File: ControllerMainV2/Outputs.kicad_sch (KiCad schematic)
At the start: 25 parts, among them IC20 TMUX6112PWR, IC27 1462039-4, J27 Conn_01x02, Q5 2N7002, T1 Lehle_MZ_P, U12 TL072

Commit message: Added libs
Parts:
- removed J26: (no value), symbol Connector_Generic:Conn_01x02
- removed J27: Conn_01x02, symbol Connector_Generic:Conn_01x02
- added C31: (no value), Capacitor_SMD:C_1206_3216Metric_Pad1.33x1.80mm_HandSolder, symbol Device:C
- added PS1: (no value), symbol SamacSys_Parts:TBA_1-0310
- added Q7: (no value), symbol SamacSys_Parts:EL817S1_A__TU_-F
- added R67: 100k, Resistor_SMD:R_1206_3216Metric_Pad1.30x1.75mm_HandSolder, symbol Device:R
- added R68: (no value), Resistor_SMD:R_1206_3216Metric_Pad1.30x1.75mm_HandSolder, symbol Device:R
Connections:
- net GND: now also PS1.1 (-VIN_(GND)), Q7.3 (E)
- net out2_con: now also Q7.4 (C), R67.2; no longer J_8.4
- net at IC27.3 (COM_1), J_8.1, R21.1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: now also J_8.4, C31.1, PS1.3 (-VOUT)
- net at J_8.5: now also Q7.2 (K)
- new net: C31.2, PS1.4 (+VOUT), R68.1
- new net: Q7.1 (A), R68.2
- new net VDD_3V3: PS1.2 (+VIN_(VCC)), R67.1
- no-connect marks 9 -> 8

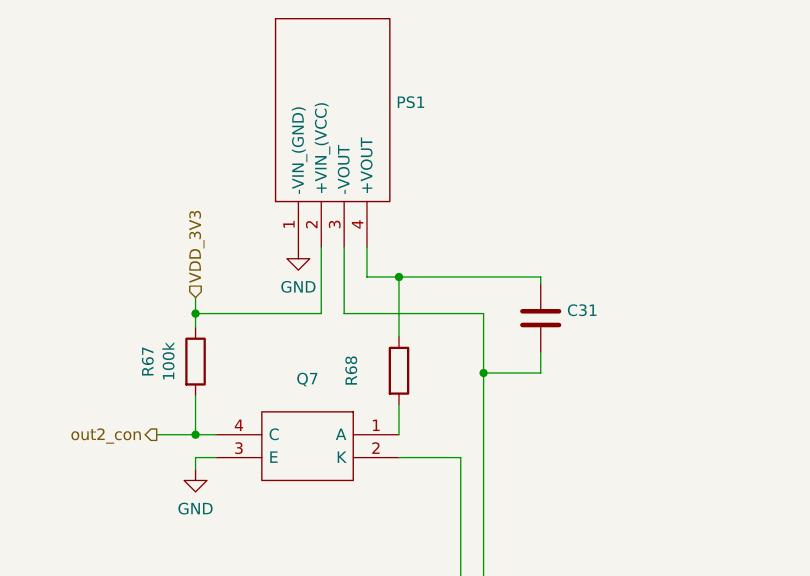
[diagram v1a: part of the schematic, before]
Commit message: Main mostly wired. Push for replacement
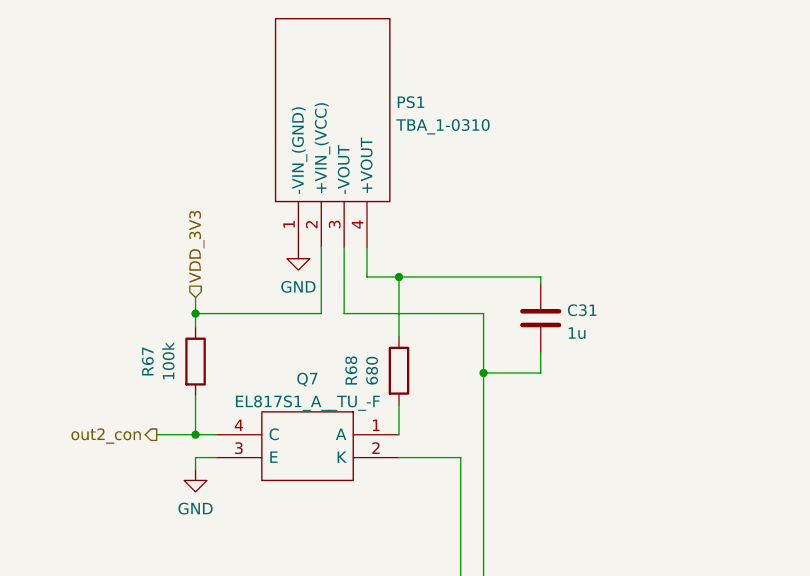
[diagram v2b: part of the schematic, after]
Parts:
- C31: value (none) -> 1u
- PS1: value (none) -> TBA_1-0310; footprint (none) -> SamacSys_Parts:TBA1
- Q7: value (none) -> EL817S1_A__TU_-F; footprint (none) -> SamacSys_Parts:SOP254P1030X390-4N
- R68: value (none) -> 680
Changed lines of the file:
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@@
     (in_bom yes) (on_board yes)
     (property "Reference" "R68" (id 0) (at 240.8682 55.372 90))
-    (property "Value" "" (id 1) (at 243.1796 55.372 90))
+    (property "Value" "680" (id 1) (at 243.1796 55.372 90))
     (property "Footprint" "Resistor_SMD:R_1206_3216Metric_Pad1.30x1.75mm_HandSolder" (id 2) (at 244.348 55.372 90)
       (effects (font (size 1.27 1.27)) hide)
@@
       (effects (font (size 1.27 1.27)) (justify right))
     )
-    (property "Value" "" (id 1) (at 245.8212 28.1182 90)
-      (effects (font (size 1.27 1.27)) (justify right))
-    )
-    (property "Footprint" "" (id 2) (at 232.41 14.986 0)
+    (property "Value" "TBA_1-0310" (id 1) (at 245.8212 28.1182 90)
+      (effects (font (size 1.27 1.27)) (justify right))
+    )
+    (property "Footprint" "SamacSys_Parts:TBA1" (id 2) (at 232.41 14.986 0)
       (effects (font (size 1.27 1.27)) (justify left) hide)
     )
@@
     (in_bom yes) (on_board yes) (fields_autoplaced)
     (property "Reference" "Q7" (id 0) (at 235.966 56.295 0))
-    (property "Value" "" (id 1) (at 235.966 58.8319 0))
-    (property "Footprint" "" (id 2) (at 229.616 59.944 0)
+    (property "Value" "EL817S1_A__TU_-F" (id 1) (at 235.966 58.8319 0))
+    (property "Footprint" "SamacSys_Parts:SOP254P1030X390-4N" (id 2) (at 229.616 59.944 0)
       (effects (font (size 1.27 1.27)) (justify left) hide)
     )
@@
       (effects (font (size 1.27 1.27)) (justify right))
     )
-    (property "Value" "" (id 1) (at 264.795 51.2322 0)
-      (effects (font (size 1.27 1.27)) (justify right))
-    )
+    (property "Value" "1u" (id 1) (at 264.795 51.2322 0)
+      (effects (font (size 1.27 1.27)) (justify right))
+    )

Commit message: Commit for branch change
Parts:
- R67: value 100k -> 10k
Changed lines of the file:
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@@
     (in_bom yes) (on_board yes)
     (property "Reference" "R67" (id 0) (at 218.2622 54.356 90))
-    (property "Value" "100k" (id 1) (at 220.5736 54.356 90))
+    (property "Value" "10k" (id 1) (at 220.5736 54.356 90))
     (property "Footprint" "Resistor_SMD:R_1206_3216Metric_Pad1.30x1.75mm_HandSolder" (id 2) (at 221.742 54.356 90)
       (effects (font (size 1.27 1.27)) hide)

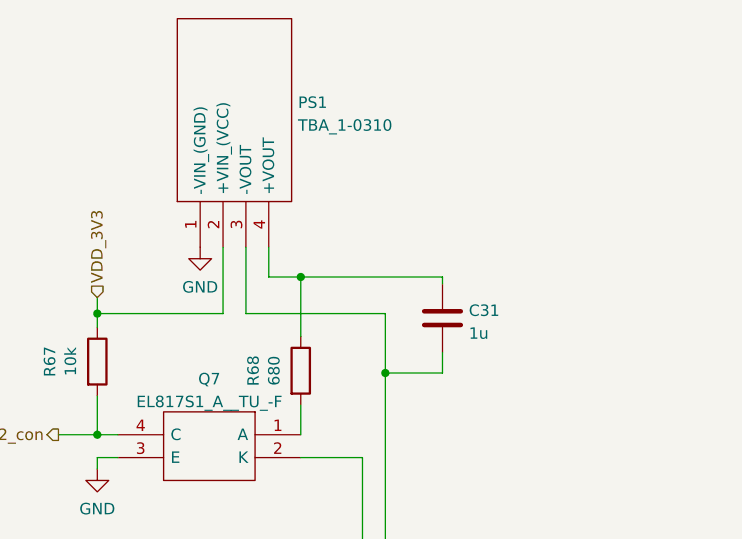
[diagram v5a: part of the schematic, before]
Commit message: Changed main to 8 loop version. Might add buffers later
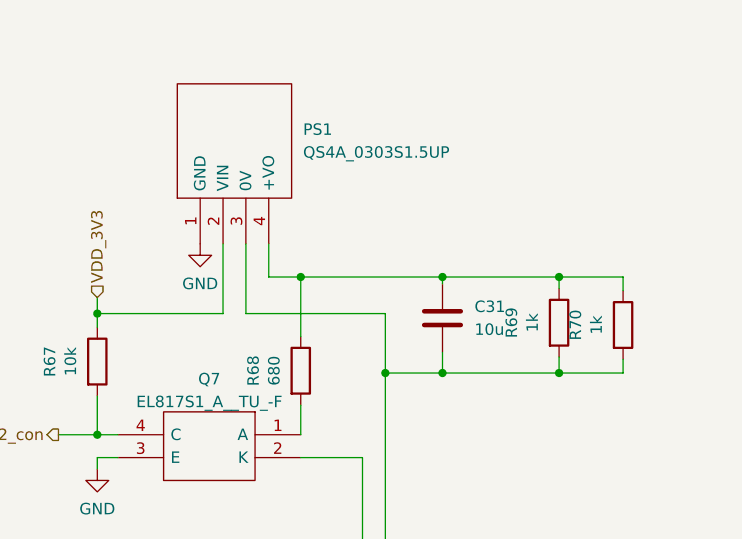
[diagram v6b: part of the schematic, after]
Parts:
- removed PS1: TBA_1-0310, SamacSys_Parts:TBA1, symbol SamacSys_Parts:TBA_1-0310
- added PS1: QS4A_0303S1.5UP, QS4A_1.5UP, symbol SamacSys_Parts:QS4A_0303S1.5UP
- added R69, R70: 1k, Resistor_SMD:R_1206_3216Metric_Pad1.30x1.75mm_HandSolder, symbol Device:R
- C31: value 1u -> 10u
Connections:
- net GND: now also PS1.1 (GND)
- net VDD_3V3: now also PS1.2 (VIN)
- net at C31.2, R68.1: now also PS1.4 (+VO), R69.1, R70.1
- net at C31.1, IC27.3 (COM_1), J_8.1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: now also PS1.3 (0V), R69.2, R70.2

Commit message: Layout of PGAs
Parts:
- PS1: footprint QS4A_1.5UP -> SamacSys_Parts:QS4A_1.5UP
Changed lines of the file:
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@@
       (effects (font (size 1.27 1.27)) (justify right))
     )
-    (property "Footprint" "QS4A_1.5UP" (id 2) (at 232.41 22.225 0)
+    (property "Footprint" "SamacSys_Parts:QS4A_1.5UP" (id 2) (at 232.41 22.225 0)
       (effects (font (size 1.27 1.27)) (justify left) hide)
     )
